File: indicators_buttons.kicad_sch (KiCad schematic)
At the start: 43 parts, among them SW1 BTN_PROGRAM, SW2 BTN_RESET, SW3 BTN_USER

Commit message: schematic wip
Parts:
- removed D10, D14: ICE BLUE, LED_SMD:LED_0603_1608Metric, symbol Device:LED
- removed D11, D13: PINK, LED_SMD:LED_0603_1608Metric, symbol Device:LED
- removed D12: WHITE, LED_SMD:LED_0603_1608Metric, symbol Device:LED
- removed R30, R36: 5.1k, Resistor_SMD:R_0402_1005Metric, symbol Device:R
- removed R32, R34, R35: 2.2k, Resistor_SMD:R_0402_1005Metric, symbol Device:R
- removed TP21, TP22, TP23, TP24, TP25: TestPoint, TestPoint:TestPoint_Pad_D1.0mm, symbol Connector:TestPoint
- C53, C54: Part Number CL05A105MQ5NNNC -> CL05A105KP5NNNC; Substitution CL05A105KQ5NNNC, CL05A105KP5NNNC, CL05A105KO5NNNC -> any equivalent
- renumbered D5 to D1, D4 to D2, D2 to D4, D1 to D5, R31 to R32
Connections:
- net +3V3: no longer R22.1
- net LED1: now also R24.2; no longer R28.2
- net LED2: now also R25.2; no longer R27.2
- net LED4: now also R27.2; no longer R25.2
- net LED5: now also R28.2; no longer R24.2
- net LED0 renamed LED6
- new net +1V8: R22.1
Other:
- note added: "Debugger LEDs 1-3"
- note added: "FPGA LEDs 4-6"
- note removed: "Debugger LEDs A-E"
- note removed: "FPGA LEDs 5-0"
- moved on the sheet: D1, D2, D3, D4, D5, D6, R24, R25, R26, R27, R28, R29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

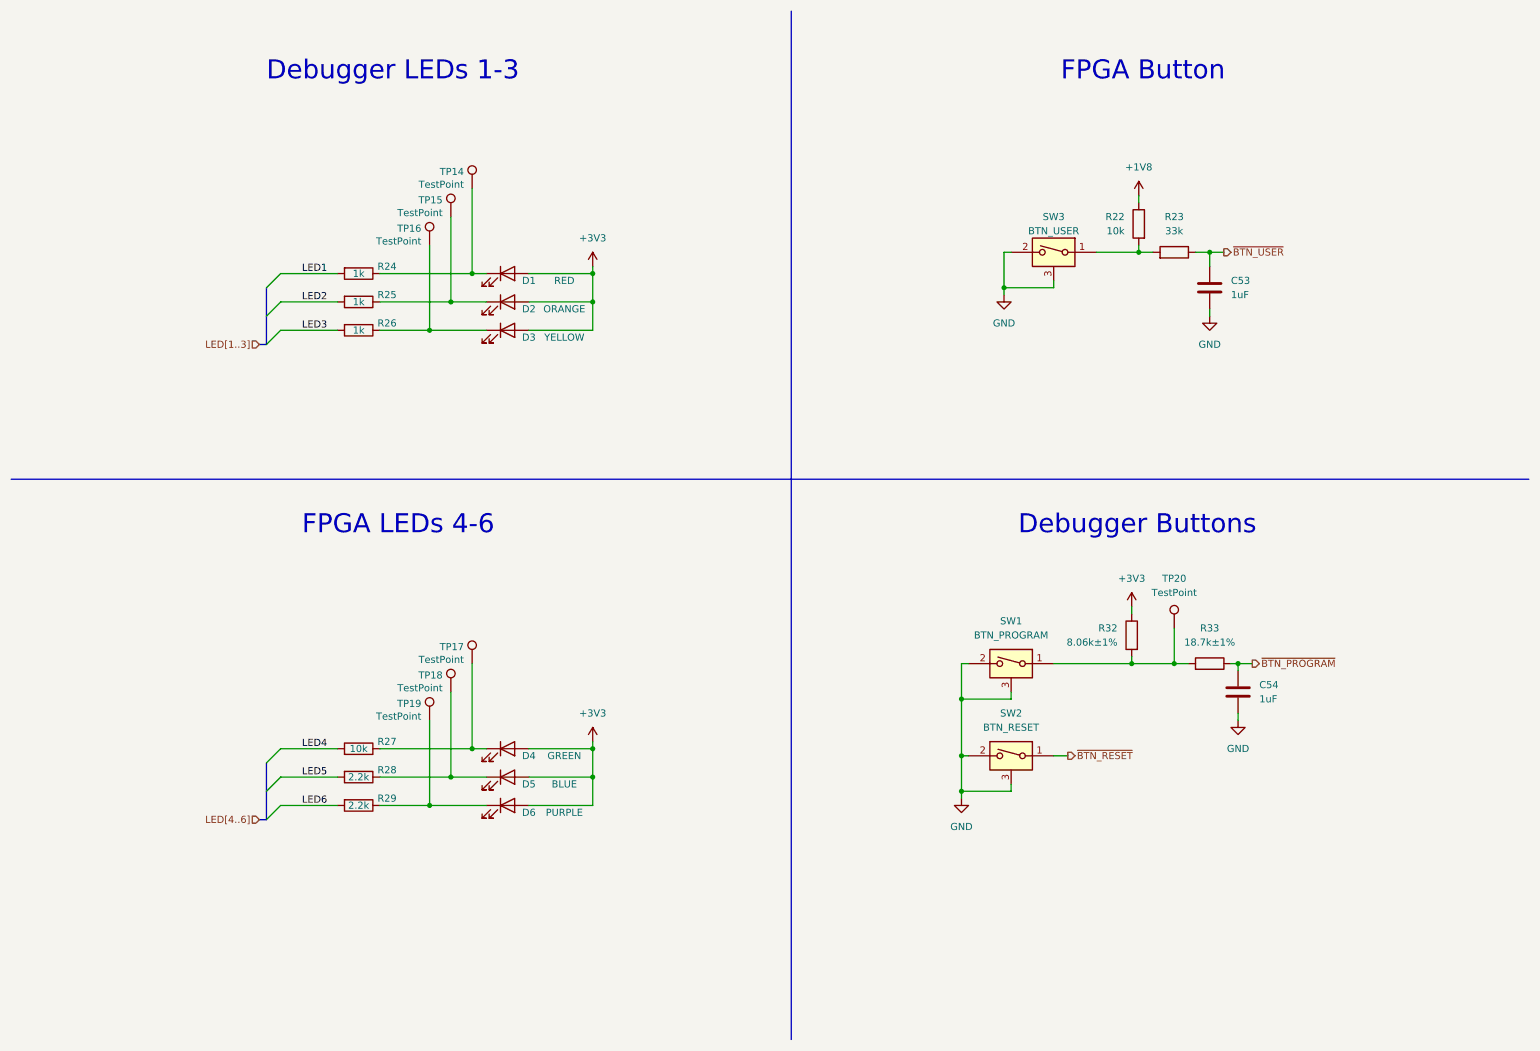
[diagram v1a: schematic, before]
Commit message: complete initial layout
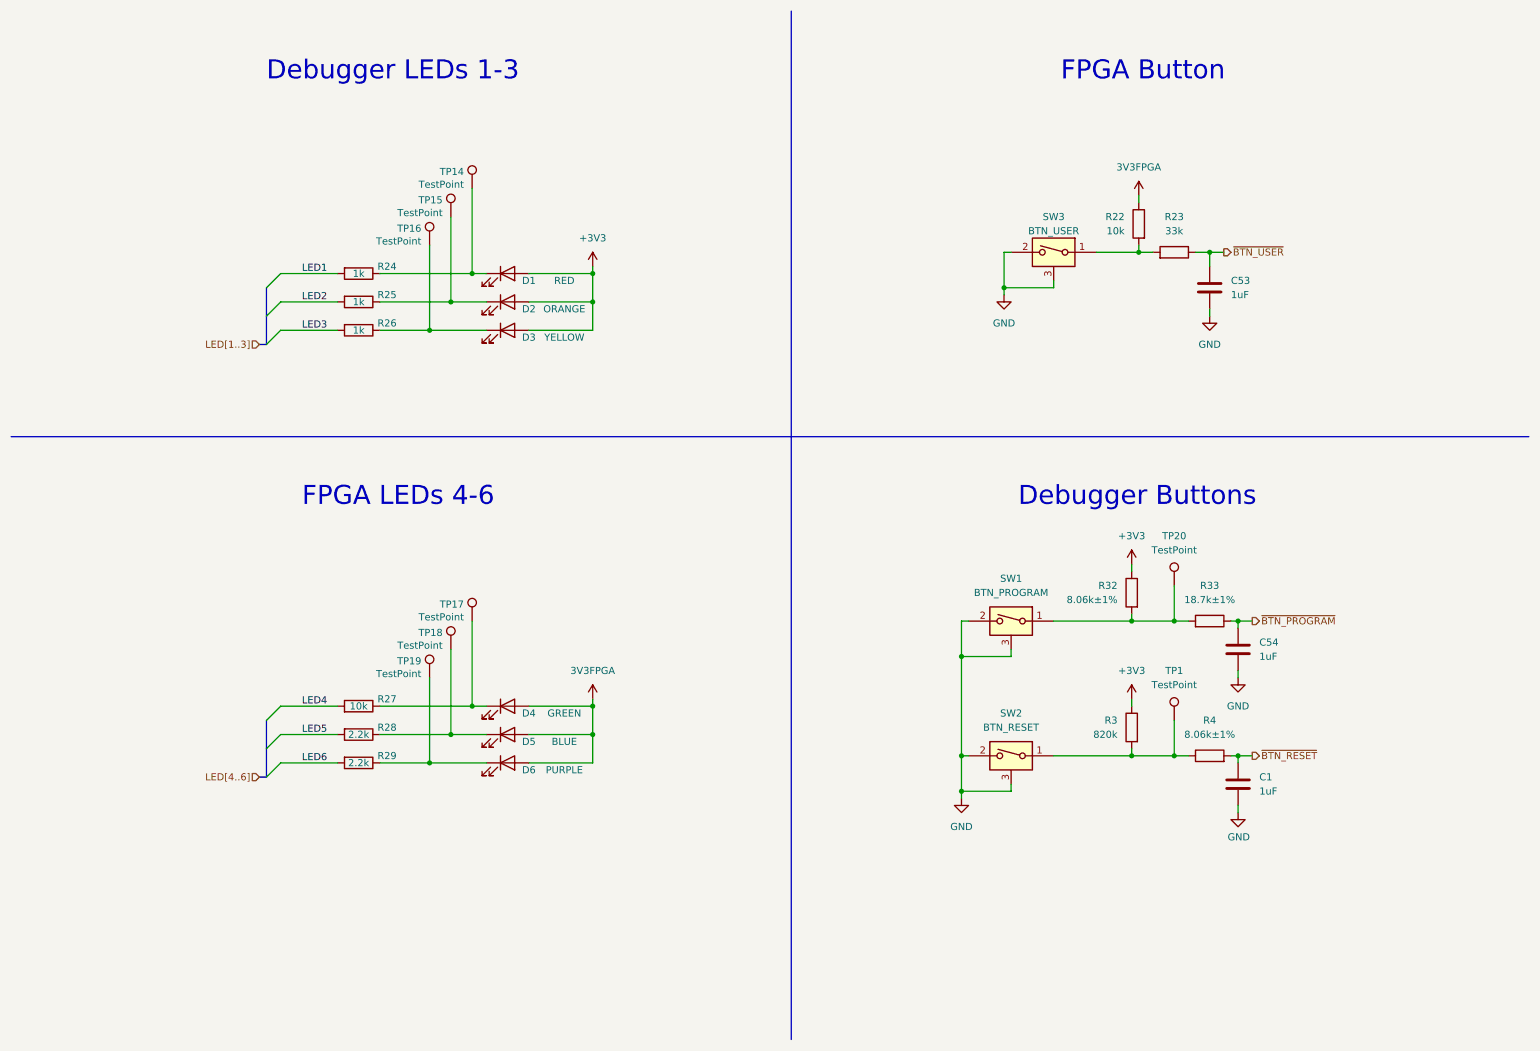
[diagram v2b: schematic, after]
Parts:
- added C1: 1uF, Capacitor_SMD:C_0402_1005Metric, symbol Device:C
- added R3: 820k, Resistor_SMD:R_0402_1005Metric, symbol Device:R
- added R4: 8.06k±1%, Resistor_SMD:R_0402_1005Metric, symbol Device:R
- added TP1: TestPoint, TestPoint:TestPoint_Pad_D1.0mm, symbol Connector:TestPoint
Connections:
- net +3V3: now also R3.1; no longer D4.2 (A), D5.2 (A), D6.2 (A)
- net GND: now also C1.2
- net ~{BTN_RESET}: now also C1.1, R4.2; no longer SW2.1
- net +1V8 renamed 3V3FPGA
- net 3V3FPGA: now also D4.2 (A), D5.2 (A), D6.2 (A)
- new net: R3.2, R4.1, SW2.1, TP1.1
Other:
- moved on the sheet: C54, D4, D5, D6, R27, R28, R29, R32, R33, SW1, TP17, TP18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
